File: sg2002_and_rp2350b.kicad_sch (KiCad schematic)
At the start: 33 parts, among them J2 Conn_01x14, J3 Conn_01x14, U10 W25Q128JVSIQTR, X3 12MHz

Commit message: Preliminary draft of USB controller and power circuit
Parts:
- removed U10: W25Q128JVSIQTR, Package_SO:SOIC-8_5.3x5.3mm_P1.27mm, symbol JLCImport:W25Q128JVSIQTR
- added CN4: W25Q128FVIQ_Connector, JLCImport:H2541FV-C762-2X04P, symbol JLCImport:H2541FV-C762-2X04P
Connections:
- net +3V3: now also CN4.8 (VCC)
- net GND: now also CN4.4 (GND)
- net PI0_QSPI_SCLK: now also CN4.6 (CLK)
- net PI0_QSPI_SD0: now also CN4.5 (D_IN)
- net PI0_QSPI_SD1: now also CN4.2 (D_OUT)
- net PI0_QSPI_SD2: now also CN4.3 (IO2)
- net PI0_QSPI_SD3: now also CN4.7 (IO3)
- net PI0_QSPI_SS: now also CN4.1 (CS#)
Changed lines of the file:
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@@
 	(wire
 		(pts
+			(xy 147.32 53.34) (xy 152.4 53.34)
+		)
+		(stroke
+			(width 0)
+			(type default)
+		)
+	)
+	(wire
+		(pts
 			(xy 43.18 256.54) (xy 67.31 256.54)
 		)
@@
 	(wire
 		(pts
+			(xy 147.32 55.88) (xy 152.4 55.88)
+		)
+		(stroke
+			(width 0)
+			(type default)
+		)
+	)
+	(wire
+		(pts
 			(xy 49.53 124.46) (xy 52.07 124.46)
 		)
@@
 	(wire
 		(pts
+			(xy 167.64 55.88) (xy 172.72 55.88)
+		)
+		(stroke
+			(width 0)
+			(type default)
+		)
+	)
+	(wire
+		(pts
 			(xy 172.72 52.07) (xy 172.72 53.34)
 		)
@@
 	(wire
 		(pts
+			(xy 167.64 60.96) (xy 172.72 60.96)
+		)
+		(stroke
+			(width 0)
+			(type default)
+		)
+	)
+	(wire
+		(pts
 			(xy 106.68 40.64) (xy 102.87 40.64)
 		)
@@
 	(wire
 		(pts
+			(xy 147.32 58.42) (xy 152.4 58.42)
+		)
+		(stroke
+			(width 0)
+			(type default)
+		)
+	)
+	(wire
+		(pts
 			(xy 87.63 228.6) (xy 133.35 228.6)
 		)
@@
 	(wire
 		(pts
+			(xy 147.32 60.96) (xy 152.4 60.96)
+		)
+		(stroke
+			(width 0)
+			(type default)
+		)
+	)
+	(wire
+		(pts
 			(xy 262.89 101.6) (xy 260.35 101.6)
 		)
@@
 	(wire
 		(pts
+			(xy 167.64 53.34) (xy 172.72 53.34)
+		)
+		(stroke
+			(width 0)
+			(type default)
+		)
+	)
+	(wire
+		(pts
 			(xy 157.48 100.33) (xy 157.48 95.25)
 		)
@@
 	(wire
 		(pts
+			(xy 167.64 58.42) (xy 172.72 58.42)
+		)
+		(stroke
+			(width 0)
+			(type default)
+		)
+	)
+	(wire
+		(pts
 			(xy 67.31 259.08) (xy 67.31 261.62)
 		)
@@
 	)
 	(symbol
+		(lib_id "JLCImport:H2541FV-C762-2X04P")
+		(at 160.02 57.15 0)
+		(unit 1)
+		(body_style 1)
+		(exclude_from_sim no)
+		(in_bom yes)
+		(on_board yes)
+		(in_pos_files yes)
+		(dnp no)
+		(property "Reference" "CN4"
+			(at 160.02 46.482 0)
+			(show_name no)
+			(do_not_autoplace no)
+			(effects
+				(font
+					(size 1.27 1.27)
+				)
+			)
+		)
+		(property "Value" "W25Q128FVIQ_Connector"
+			(at 160.02 49.022 0)
+			(show_name no)
+			(do_not_autoplace no)
+			(effects
+				(font
+					(size 0.8128 0.8128)
+				)
+			)
+		)
+		(property "Footprint" "JLCImport:H2541FV-C762-2X04P"
+			(at 160.02 57.15 0)
+			(hide yes)
+			(show_name no)
+			(do_not_autoplace no)
+			(effects
+				(font
+					(size 1.27 1.27)
+				)
+			)
+		)
+		(property "Datasheet" "https://www.lcsc.com/datasheet/lcsc_datasheet_2405141422_HanElectricity-H2541FV-C762-2x04P_C22387106.pdf"
+			(at 160.02 57.15 0)
+			(hide yes)
+			(show_name no)
+			(do_not_autoplace no)
+			(effects
+				(font
+					(size 1.27 1.27)
+				)
+			)
+		)
+		(property "Description" "-55℃~+105℃ 2.54mm 7.62mm 8P DIP Phosphor bronze Square Hole DIP-8 IC / Transistor Socket ROHS"
+			(at 160.02 57.15 0)
+			(hide yes)
+			(show_name no)
+			(do_not_autoplace no)
+			(effects
+				(font
+					(size 1.27 1.27)
+				)
+			)
+		)
+		(property "LCSC" "C22387106"
+			(at 160.02 57.15 0)
+			(hide yes)
+			(show_name no)
+			(do_not_autoplace no)
+			(effects
+				(font
+					(size 1.27 1.27)
+				)
+			)
+		)
+		(property "Manufacturer" "HanElectricity"
+			(at 160.02 57.15 0)
+			(hide yes)
+			(show_name no)
+			(do_not_autoplace no)
+			(effects
+				(font
+					(size 1.27 1.27)
+				)
+			)
+		)
+		(property "Manufacturer Part" "H2541FV-C762-2x04P"
+			(at 160.02 57.15 0)
+			(hide yes)
+			(show_name no)
+			(do_not_autoplace no)
+			(effects
+				(font
+					(size 1.27 1.27)
+				)
+			)
+		)
+		(pin "2"
+		)
+		(pin "1"
+		)
+		(pin "8"
+		)
+		(pin "3"
+		)
+		(pin "5"
+		)
+		(pin "7"
+		)
+		(pin "4"
+		)
+		(pin "6"
+		)
+		(instances
+			(project "serverv2_backplane"
+				(path "/1fa8d8fa-b9bb-45b7-bc88-3b533c66ef8d"
+					(reference "CN4")
+					(unit 1)
+				)
+			)
+		)
+	)
+	(symbol
 		(lib_id "JLCImport:CL05B104KB54PNC")
 		(at 124.46 160.02 90)
@@
 					(unit 1)
 				)
-			)
-		)
-	)
-	(symbol
-		(lib_id "JLCImport:W25Q128JVSIQTR")
-		(at 160.02 57.15 0)
-		(unit 1)
-		(body_style 1)
-		(exclude_from_sim no)
-		(in_bom yes)
-		(on_board yes)
-		(in_pos_files yes)
-		(dnp no)
-		(fields_autoplaced yes)
-		(property "Reference" "U10"
-			(at 160.02 45.72 0)
-			(show_name no)
-			(do_not_autoplace no)
-			(effects
-				(font
-					(size 1.27 1.27)
-				)
-			)
-		)
-		(property "Value" "W25Q128JVSIQTR"
-			(at 160.02 48.26 0)
-			(show_name no)
-			(do_not_autoplace no)
-			(effects
-				(font
-					(size 1.27 1.27)
-				)
-			)
-		)
-		(property "Footprint" "Package_SO:SOIC-8_5.3x5.3mm_P1.27mm"
-			(at 160.02 57.15 0)
-			(hide yes)
-			(show_name no)
-			(do_not_autoplace no)
-			(effects
-				(font
-					(size 1.27 1.27)
-				)
-			)
-		)
-		(property "Datasheet" "https://www.lcsc.com/datasheet/lcsc_datasheet_1811142111_Winbond-Elec-W25Q128JVSIQ_C97521.pdf"
-			(at 160.02 57.15 0)
-			(hide yes)
-			(show_name no)
-			(do_not_autoplace no)
-			(effects
-				(font
-					(size 1.27 1.27)
-				)
-			)
-		)
-		(property "Description" "-40℃~+85℃ 100,000 cycles 120ms@(32KB) 128Mbit 133MHz 1uA 2.7V~3.6V 20 Years 3ms SPI SOIC-8-208mil NOR FLASH ROHS"
-			(at 160.02 57.15 0)
-			(hide yes)
-			(show_name no)
-			(do_not_autoplace no)
-			(effects
-				(font
-					(size 1.27 1.27)
-				)
-			)
-		)
-		(property "LCSC" "C97521"
-			(at 160.02 57.15 0)
-			(hide yes)
-			(show_name no)
-			(do_not_autoplace no)
-			(effects
-				(font
-					(size 1.27 1.27)
-				)
-			)
-		)
-		(property "Manufacturer" "Winbond Elec"
-			(at 160.02 57.15 0)
-			(hide yes)
-			(show_name no)
-			(do_not_autoplace no)
-			(effects
-				(font
-					(size 1.27 1.27)
-				)
-			)
-		)
-		(property "Manufacturer Part" "W25Q128JVSIQ"
-			(at 160.02 57.15 0)
-			(hide yes)
-			(show_name no)
-			(do_not_autoplace no)
-			(effects
-				(font
-					(size 1.27 1.27)
-				)
-			)
-		)
-		(pin "3"
-		)
-		(pin "4"
-		)
-		(pin "7"
-		)
-		(pin "8"
-		)
-		(pin "2"
-		)
-		(pin "5"
-		)
-		(pin "6"
-		)
-		(pin "1"
-		)
-		(instances
-			(project "serverv2_backplane"
-				(path "/1fa8d8fa-b9bb-45b7-bc88-3b533c66ef8d"
-					(reference "U10")
-					(unit 1)
-				)

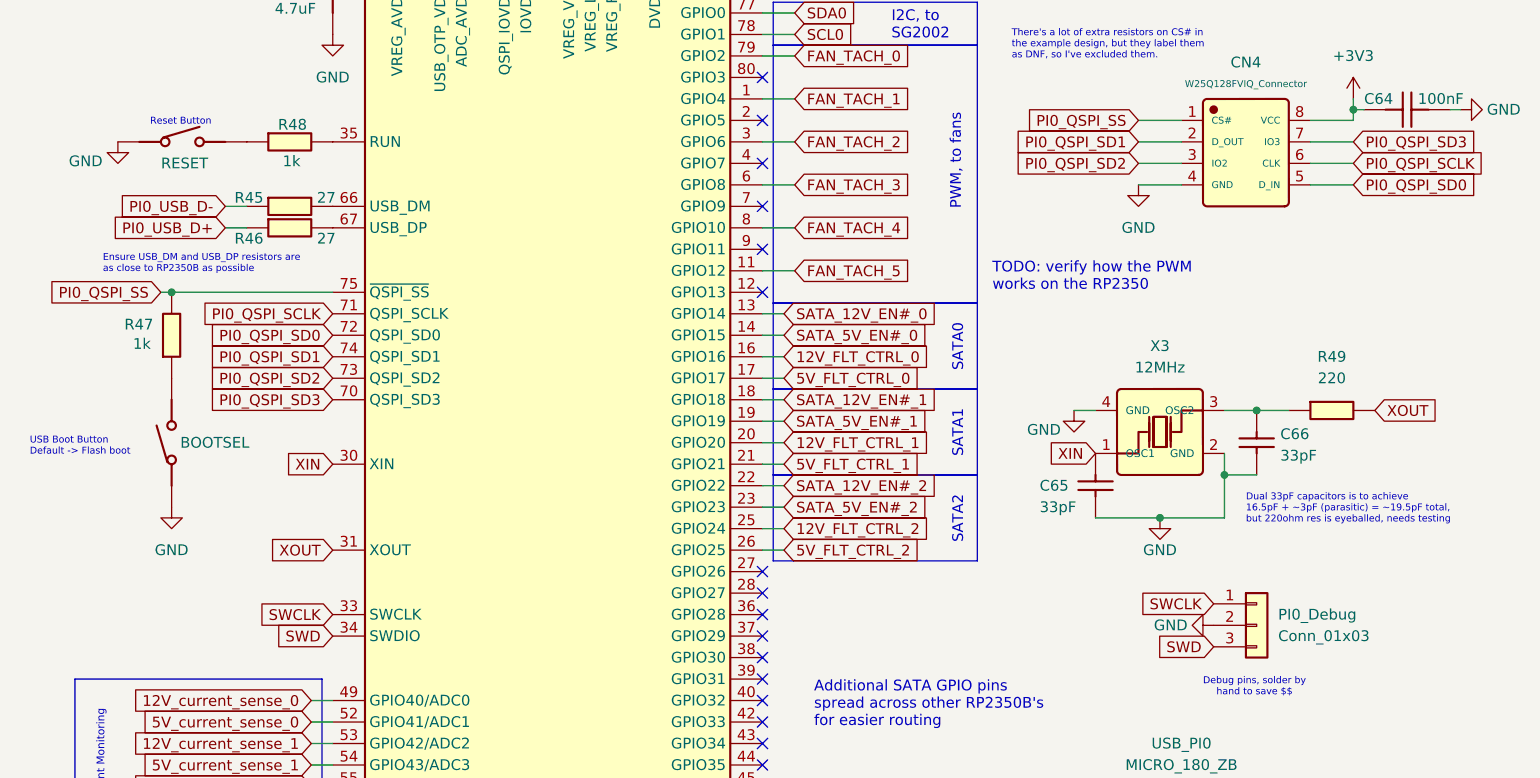
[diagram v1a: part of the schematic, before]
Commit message: Preliminary revision of USB hub and temperature monitor
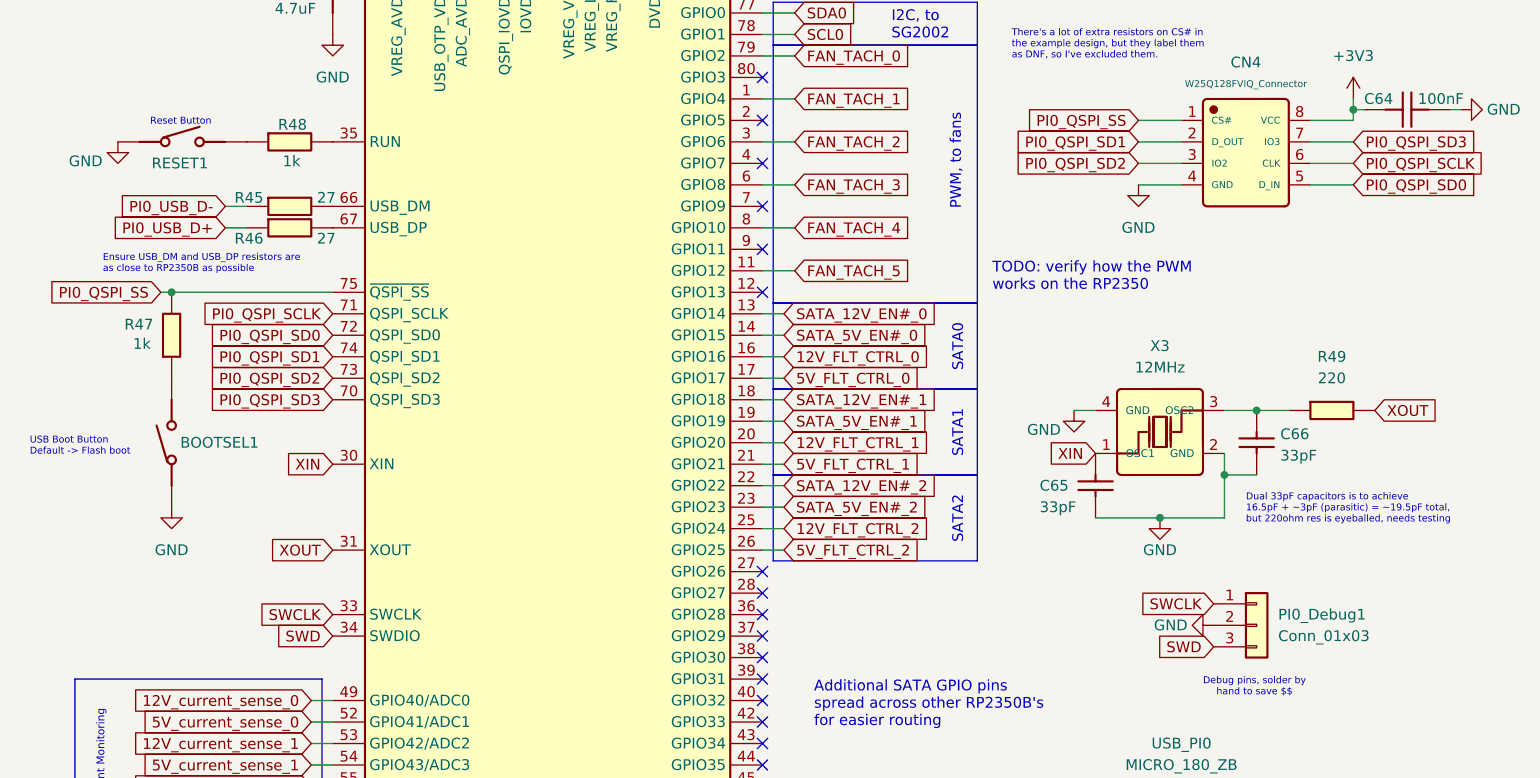
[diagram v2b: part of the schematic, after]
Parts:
- renumbered BOOTSEL to BOOTSEL1, PI0_Debug to PI0_Debug1, RESET to RESET1
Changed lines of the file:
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@@
 		(in_pos_files yes)
 		(dnp no)
-		(property "Reference" "RESET"
+		(property "Reference" "RESET1"
 			(at 37.338 58.42 0)
 			(show_name no)
@@
 			(project "serverv2_backplane"
 				(path "/1fa8d8fa-b9bb-45b7-bc88-3b533c66ef8d"
-					(reference "RESET")
+					(reference "RESET1")
 					(unit 1)
 				)
@@
 		(dnp no)
 		(fields_autoplaced yes)
-		(property "Reference" "PI0_Debug"
+		(property "Reference" "PI0_Debug1"
 			(at 163.83 111.7599 0)
 			(show_name no)
@@
 			(project "serverv2_backplane"
 				(path "/1fa8d8fa-b9bb-45b7-bc88-3b533c66ef8d"
-					(reference "PI0_Debug")
+					(reference "PI0_Debug1")
 					(unit 1)
 				)
@@
 		(in_pos_files yes)
 		(dnp no)
-		(property "Reference" "BOOTSEL"
+		(property "Reference" "BOOTSEL1"
 			(at 34.036 91.44 90)
 			(show_name no)
@@
 			(project "serverv2_backplane"
 				(path "/1fa8d8fa-b9bb-45b7-bc88-3b533c66ef8d"
-					(reference "BOOTSEL")
+					(reference "BOOTSEL1")
 					(unit 1)
 				)

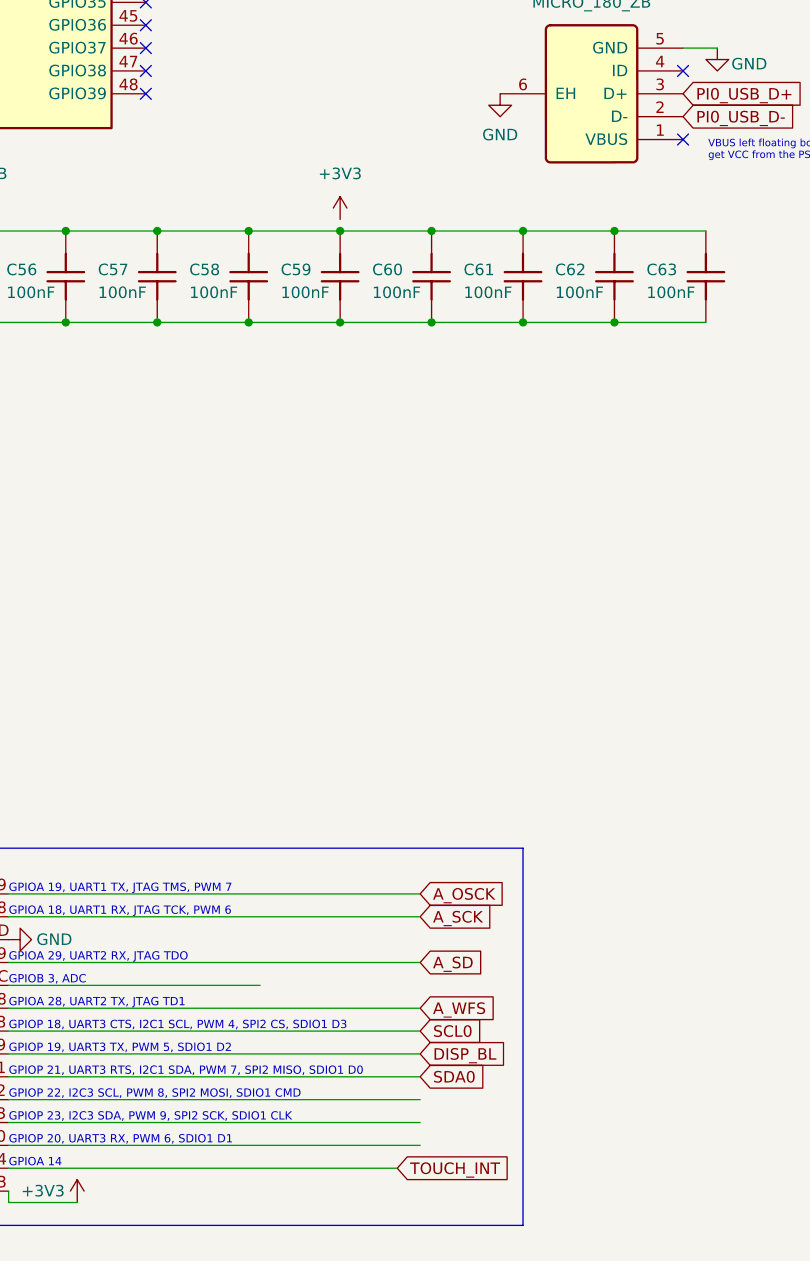
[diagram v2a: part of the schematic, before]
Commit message: Preliminary design of power monitor for PSU rails and USB-C VBUS
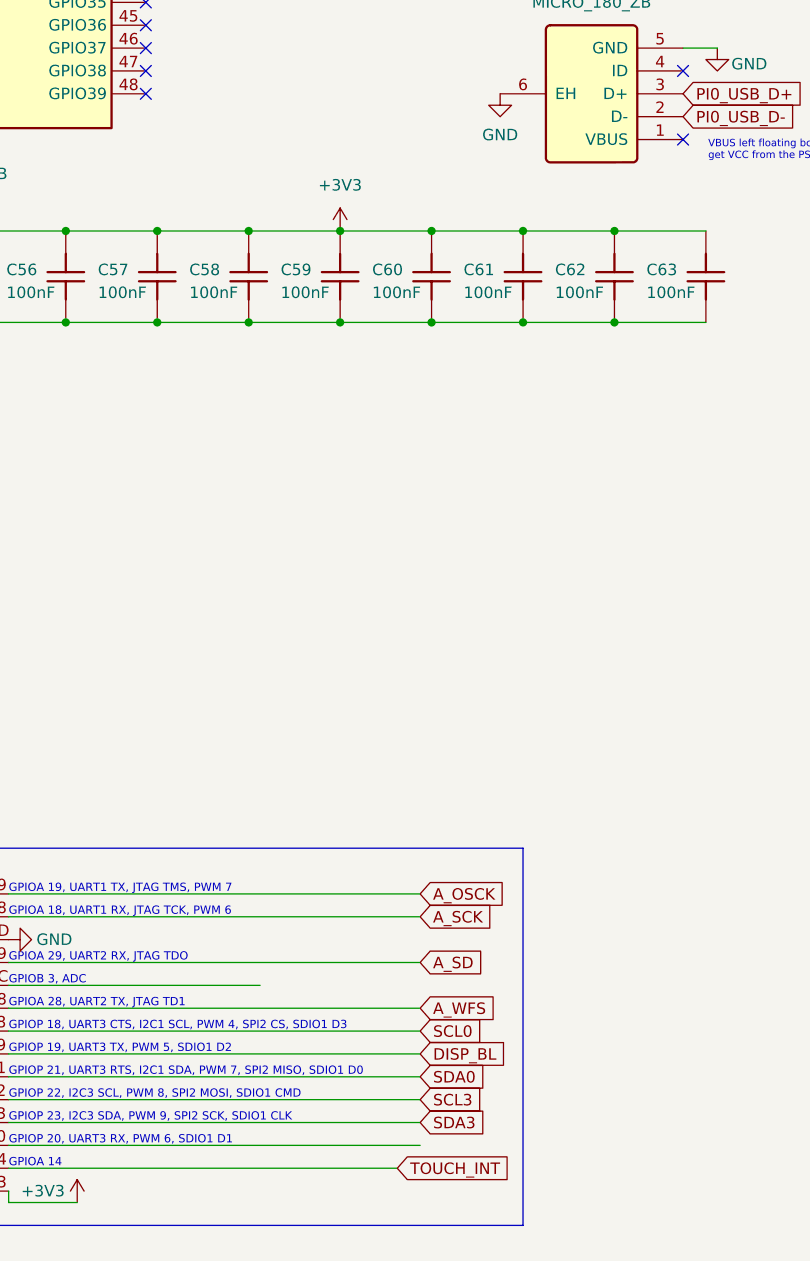
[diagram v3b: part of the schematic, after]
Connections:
- net +3V3: now also C55.2, C56.2, C57.2, C58.2, C59.2, C60.2, C61.2, C62.2, C63.2
- net SCL3: now reaches J3.P22 (Pin_5)
- net SDA3: now reaches J3.P23 (Pin_4)
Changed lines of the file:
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@@
+		)
+	)
+	(global_label "SCL3"
+		(shape input)
+		(at 133.35 251.46 0)
+		(fields_autoplaced yes)
+		(effects
+			(font
+				(size 1.27 1.27)
+			)
+			(justify left)
+		)
+		(property "Intersheetrefs" "${INTERSHEET_REFS}"
+			(at 141.0523 251.46 0)
+			(hide yes)
+			(show_name no)
+			(do_not_autoplace no)
+			(effects
+				(font
+					(size 1.27 1.27)
+				)
+				(justify left)
+			)
 		)
 	)
@@
 				)
 				(justify right)
+			)
+		)
+	)
+	(global_label "SDA3"
+		(shape input)
+		(at 133.35 254 0)
+		(fields_autoplaced yes)
+		(effects
+			(font
+				(size 1.27 1.27)
+			)
+			(justify left)
+		)
+		(property "Intersheetrefs" "${INTERSHEET_REFS}"
+			(at 141.1128 254 0)
+			(hide yes)
+			(show_name no)
+			(do_not_autoplace no)
+			(effects
+				(font
+					(size 1.27 1.27)
+				)
+				(justify left)
 			)
 		)
@@
 	(symbol
 		(lib_id "power:+3V3")
-		(at 124.46 153.67 0)
+		(at 124.46 154.94 0)
 		(unit 1)
 		(body_style 1)
@@
 		(fields_autoplaced yes)
 		(property "Reference" "#PWR0131"
-			(at 124.46 157.48 0)
+			(at 124.46 158.75 0)
 			(hide yes)
 			(show_name no)
@@
 		)
 		(property "Value" "+3V3"
-			(at 124.46 148.59 0)
+			(at 124.46 149.86 0)
 			(show_name no)
 			(do_not_autoplace no)
@@
 		)
 		(property "Footprint" ""
-			(at 124.46 153.67 0)
+			(at 124.46 154.94 0)
 			(hide yes)
 			(show_name no)
@@
 		)
 		(property "Datasheet" ""
-			(at 124.46 153.67 0)
+			(at 124.46 154.94 0)
 			(hide yes)
 			(show_name no)
@@
 		)
 		(property "Description" "Power symbol creates a global label with name \"+3V3\""
-			(at 124.46 153.67 0)
-			(hide yes)
-			(show_name no)
+			(at 124.46 154.94 0)
+			(hide yes)
+			(show_name no)

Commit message: Preliminary design of power monitor for PS176, TC358743, LicheeRV nano, and touch display
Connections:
- net +5V renamed +5V_SG2002
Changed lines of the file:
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@@
 	)
 	(junction
+		(at 67.31 261.62)
+		(diameter 0)
+		(color 0 0 0 0)
+	)
+	(junction
 		(at 33.02 73.66)
 		(diameter 0)
@@
 	)
 	(junction
-		(at 67.31 261.62)
-		(diameter 0)
-		(color 0 0 0 0)
-	)
-	(junction
 		(at 172.72 52.07)
 		(diameter 0)
@@
 	(wire
 		(pts
-			(xy 60.96 261.62) (xy 67.31 261.62)
+			(xy 53.34 261.62) (xy 67.31 261.62)
 		)
 		(stroke
@@
 	(symbol
 		(lib_id "power:+5V")
-		(at 60.96 261.62 0)
+		(at 53.34 261.62 0)
 		(unit 1)
 		(body_style 1)
@@
 		(dnp no)
 		(property "Reference" "#PWR073"
-			(at 60.96 265.43 0)
+			(at 53.34 265.43 0)
 			(hide yes)
 			(show_name no)
@@
 			)
 		)
-		(property "Value" "+5V"
-			(at 64.008 260.35 0)
+		(property "Value" "+5V_SG2002"
+			(at 60.452 260.35 0)
 			(show_name no)
 			(do_not_autoplace no)
@@
 		)
 		(property "Footprint" ""
-			(at 60.96 261.62 0)
+			(at 53.34 261.62 0)
 			(hide yes)
 			(show_name no)
@@
 		)
 		(property "Datasheet" ""
-			(at 60.96 261.62 0)
+			(at 53.34 261.62 0)
 			(hide yes)
 			(show_name no)
@@
 		)
 		(property "Description" "Power symbol creates a global label with name \"+5V\""
-			(at 60.96 261.62 0)
+			(at 53.34 261.62 0)
 			(hide yes)
 			(show_name no)
